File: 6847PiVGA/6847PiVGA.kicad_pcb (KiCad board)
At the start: 2 copper layers, 37 parts, among them J1 DB15_Female_HighDensity, U1 MC6847, U2 AD724JRZ, U4 AD813, Y1 4.433620MHz

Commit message: refine hardware layout
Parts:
- added U3: Pico, Package_DIP:DIP-42_W15.24mm, F.Cu at (90.9, 86.1)
- J1: footprint Resistor_SMD:R_0603_1608Metric -> Connector_Dsub:DSUB-15-HD_Female_Horizontal_P2.29x1.98mm_EdgePinOffset3.03mm_Housed_MountingHolesOffset4.94mm
- moved R6 79.6 mm to (111.8, 125.2), turned to 180 degrees
- moved C2 76.6 mm to (125.1, 133.7), turned to 180 degrees
- moved C8 75.0 mm to (126.4, 129.9), turned to 180 degrees
- moved R4 74.9 mm to (111.8, 119.1), turned to 180 degrees
- moved R12 74.7 mm to (115.8, 129.5)
- moved R2 72.1 mm to (111.8, 109.5), turned to 180 degrees
- moved U4 72.0 mm to (131.8, 107.2)
- moved R13 66.3 mm to (146.2, 135.0), turned to -90 degrees
- moved R5 66.1 mm to (111.8, 122.2), turned to 180 degrees
- moved R7 62.8 mm to (111.8, 129.5), turned to 180 degrees
- moved R9 59.9 mm to (111.8, 135.6), turned to 180 degrees
- moved C3 57.9 mm to (122.6, 132.0), turned to 180 degrees
- moved C4 57.5 mm to (122.0, 116.1)
- moved C9 55.4 mm to (146.2, 131.4), turned to -90 degrees
- moved C7 55.0 mm to (125.9, 119.3)
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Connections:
- C1 pad 2: Net-(C1-Pad2) -> Net-(J1-Pad3)
- C3 pad 2: Net-(C3-Pad2) -> Net-(J1-Pad1)
- J1 pad 1: Net-(C3-Pad2) -> Net-(J1-Pad1)
- R1 pad 1: Net-(C1-Pad2) -> Net-(J1-Pad1)
- R10 pad 1: Net-(C1-Pad2) -> Net-(J1-Pad1)
- R12 pad 1: Net-(C3-Pad2) -> Net-(J1-Pad3)
- R2 pad 1: Net-(C1-Pad2) -> Net-(J1-Pad1)
- R3 pad 1: Net-(C1-Pad2) -> Net-(J1-Pad1)
- R7 pad 1: Net-(C3-Pad2) -> Net-(J1-Pad3)
- R8 pad 1: Net-(C3-Pad2) -> Net-(J1-Pad3)
- R9 pad 1: Net-(C3-Pad2) -> Net-(J1-Pad3)
- U4 pad 10: Net-(C3-Pad2) -> Net-(J1-Pad3)
- U4 pad 5: Net-(C1-Pad2) -> Net-(J1-Pad1)
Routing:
- net +5V: track 0.00 -> 194.8 mm, vias 0 -> 2
- net Net-(J1-Pad14): track 0.00 -> 136.5 mm, vias 0 -> 2
- net Net-(J1-Pad13): track 0.00 -> 130.7 mm, vias 0 -> 3
- net GND: track 0.00 -> 84.7 mm, vias 0 -> 12
- net Net-(J1-Pad3): track 0.00 -> 84.1 mm, vias 0 -> 3
- net Net-(J1-Pad2): track 0.00 -> 80.2 mm, vias 0 -> 4
- net Net-(J1-Pad1): track 0.00 -> 72.5 mm, vias 0 -> 3
- net Net-(U1-Pad35): track 0.00 -> 41.1 mm
- net Net-(U1-Pad39): track 0.00 -> 37.8 mm
- net Net-(U1-Pad2): track 0.00 -> 33.5 mm
- net Net-(U1-Pad33): track 0.00 -> 28.0 mm
- net Net-(U1-Pad34): track 0.00 -> 27.0 mm
- net Net-(R19-Pad2): track 0.00 -> 13.1 mm
- net Net-(R18-Pad2): track 0.00 -> 12.9 mm
- net Net-(R17-Pad2): track 0.00 -> 11.1 mm
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- added copper zone on F.Cu, net GND
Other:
- board outline added: 69.6 x 59.2 mm

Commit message: board refresh
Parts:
- C1, C10, C2, C3, C4, C5, C6, C7, C8, C9: footprint Capacitor_SMD:C_0603_1608Metric -> Capacitor_SMD:C_0805_2012Metric
- R1, R10, R11, R12, R13, R14, R15, R16, R17, R18, R19, R20, R21, R22, R5, R8: footprint Resistor_SMD:R_0603_1608Metric -> Resistor_SMD:R_0805_2012Metric
- R2: value 1K -> 2K; footprint Resistor_SMD:R_0603_1608Metric -> Resistor_SMD:R_0805_2012Metric
- R3, R6, R9: value 2K -> 499R; footprint Resistor_SMD:R_0603_1608Metric -> Resistor_SMD:R_0805_2012Metric
- R4, R7: value 499R -> 2K; footprint Resistor_SMD:R_0603_1608Metric -> Resistor_SMD:R_0805_2012Metric
- moved R20 29.7 mm to (142.6, 91.9), turned to 180 degrees
- moved R17 25.3 mm to (142.6, 96.0)
- moved R14 24.9 mm to (142.6, 94.0), turned to 0 degrees
- moved R9 6.35 mm to (111.7, 129.3)
- moved R1 6.10 mm to (111.7, 112.5)
- moved R3 6.10 mm to (111.8, 106.4)
- moved R4 6.10 mm to (111.8, 125.2)
- moved R6 6.10 mm to (111.8, 119.1)
- moved R7 5.84 mm to (111.7, 135.4)
- moved R16 3.33 mm to (142.6, 111.8)
- moved R15 3.30 mm to (142.6, 102.7)
- moved R19 1.78 mm to (142.7, 114.3)
- moved R21 1.27 mm to (142.7, 100.6)
- moved C9 0.89 mm to (145.3, 131.4)
- moved R13 0.89 mm to (145.3, 135.0)
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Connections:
- net Net-(C1-Pad1) renamed /Bin
- net Net-(C2-Pad1) renamed /Gin
- net Net-(C3-Pad1) renamed /Rin
- net Net-(C9-Pad1) renamed /Composite
- net Net-(J1-Pad1) renamed Rvga
- net Net-(J1-Pad2) renamed Gvga
- net Net-(J1-Pad3) renamed Bvga
- net Net-(U1-Pad2) renamed DD6
- net Net-(U1-Pad22) renamed Atiming
- net Net-(U1-Pad27) renamed GM2
- net Net-(U1-Pad29) renamed GM1
- net Net-(U1-Pad3) renamed DD0
- net Net-(U1-Pad30) renamed GM0
- net Net-(U1-Pad33) renamed CLK
- net Net-(U1-Pad34) renamed DD7
- net Net-(U1-Pad35) renamed ~{A}/G
- net Net-(U1-Pad39) renamed CSS
- net Net-(U1-Pad4) renamed DD1
- net Net-(U1-Pad5) renamed DD2
- net Net-(U1-Pad6) renamed DD3
- net Net-(U1-Pad7) renamed DD4
- net Net-(U1-Pad8) renamed DD5
- J1 pad 10: unconnected-(J1-Pad10) -> GND
- J1 pad 13: Net-(J1-Pad13) -> Hsync
- J1 pad 14: Net-(J1-Pad14) -> Vsync
- J1 pad 5: unconnected-(J1-Pad5) -> GND
- J1 pad 7: unconnected-(J1-Pad7) -> GND
- U1 pad 12: Net-(J1-Pad13) -> Vsync
- U1 pad 37: Net-(J1-Pad13) -> Vsync
- U1 pad 38: Net-(J1-Pad14) -> Hsync
- U2 pad 15: Net-(J1-Pad13) -> Vsync
- U2 pad 16: Net-(J1-Pad14) -> Hsync
- U3 pad 17: Net-(J1-Pad13) -> Vsync
- U3 pad 18: unconnected-(U3-Pad18) -> GND
- U3 pad 21: Net-(J1-Pad14) -> Hsync
- U3 pad 22: Net-(R9-Pad2) -> Net-(R7-Pad2)
- U3 pad 23: unconnected-(U3-Pad23) -> GND
- U3 pad 25: Net-(R7-Pad2) -> Net-(R9-Pad2)
- U3 pad 26: Net-(R6-Pad2) -> Net-(R4-Pad2)
- U3 pad 28: unconnected-(U3-Pad28) -> GND
- U3 pad 29: Net-(R4-Pad2) -> Net-(R6-Pad2)
- U3 pad 3: unconnected-(U3-Pad3) -> GND
- U3 pad 31: Net-(R3-Pad2) -> Net-(R1-Pad2)
- U3 pad 33: unconnected-(U3-Pad33) -> GND
- U3 pad 34: Net-(R1-Pad2) -> Net-(R3-Pad2)
- U3 pad 39: unconnected-(U3-Pad39) -> +5V
- U3 pad 40: +5V -> unconnected-(U3-Pad40)
- U3 pad 8: unconnected-(U3-Pad8) -> GND
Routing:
- net GND: track 84.7 -> 223.6 mm
- net Net-(J1-Pad14): track 136.5 -> 0.00 mm, vias 2 -> 0
- net Hsync: track 0.00 -> 134.2 mm, vias 0 -> 2
- net Vsync: track 0.00 -> 133.1 mm, vias 0 -> 3
- net Net-(J1-Pad13): track 130.7 -> 0.00 mm, vias 3 -> 0
- net Net-(R14-Pad1): track 7.93 -> 27.1 mm, vias 0 -> 2
- net Net-(R17-Pad2): track 11.1 -> 29.4 mm, vias 0 -> 2
- net Net-(R19-Pad2): track 13.1 -> 15.9 mm
- net Net-(R16-Pad1): track 8.25 -> 10.0 mm
- net Net-(R15-Pad1): track 8.25 -> 9.92 mm
- net Bvga: track 84.1 -> 85.3 mm
- net /Composite: track 4.24 -> 3.19 mm
- net Rvga: track 72.5 -> 71.5 mm
- net Net-(R18-Pad2): track 12.9 -> 13.9 mm
- net Gvga: track 80.2 -> 81.2 mm
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
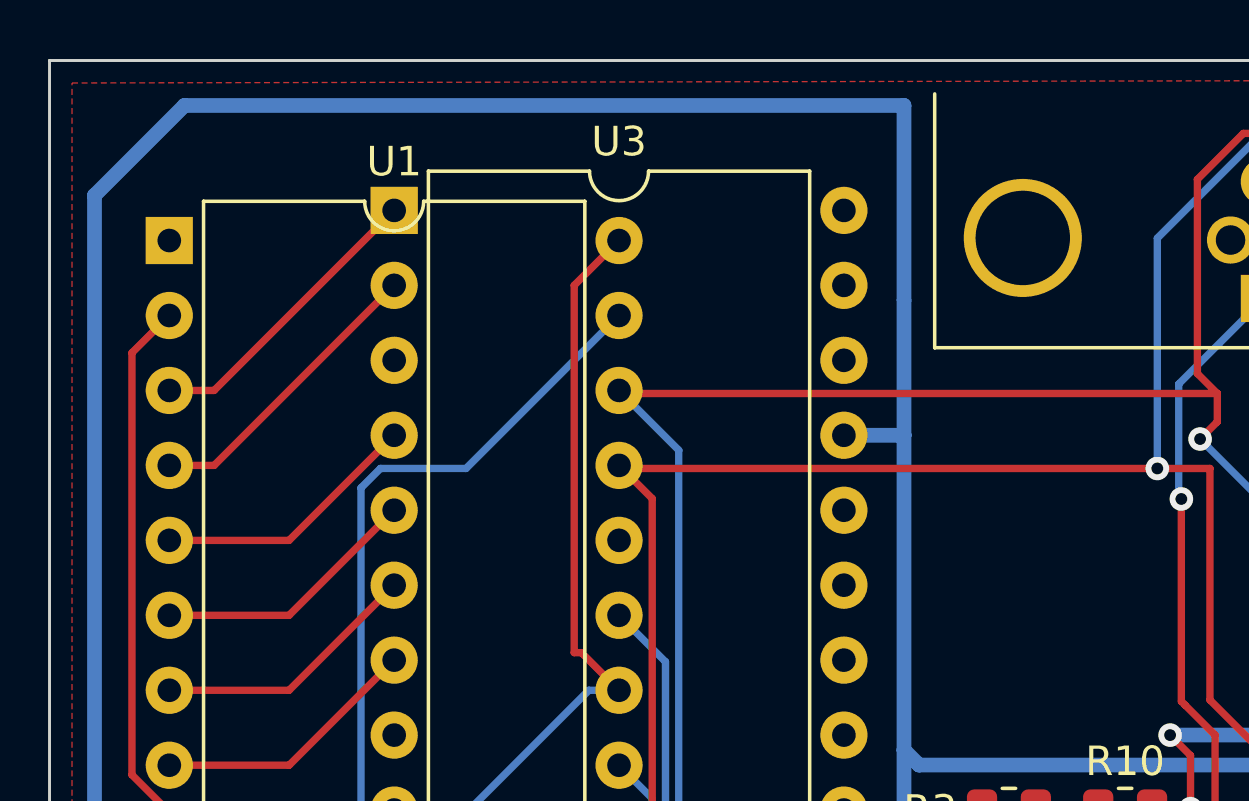
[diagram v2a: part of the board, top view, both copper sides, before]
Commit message: add power protection
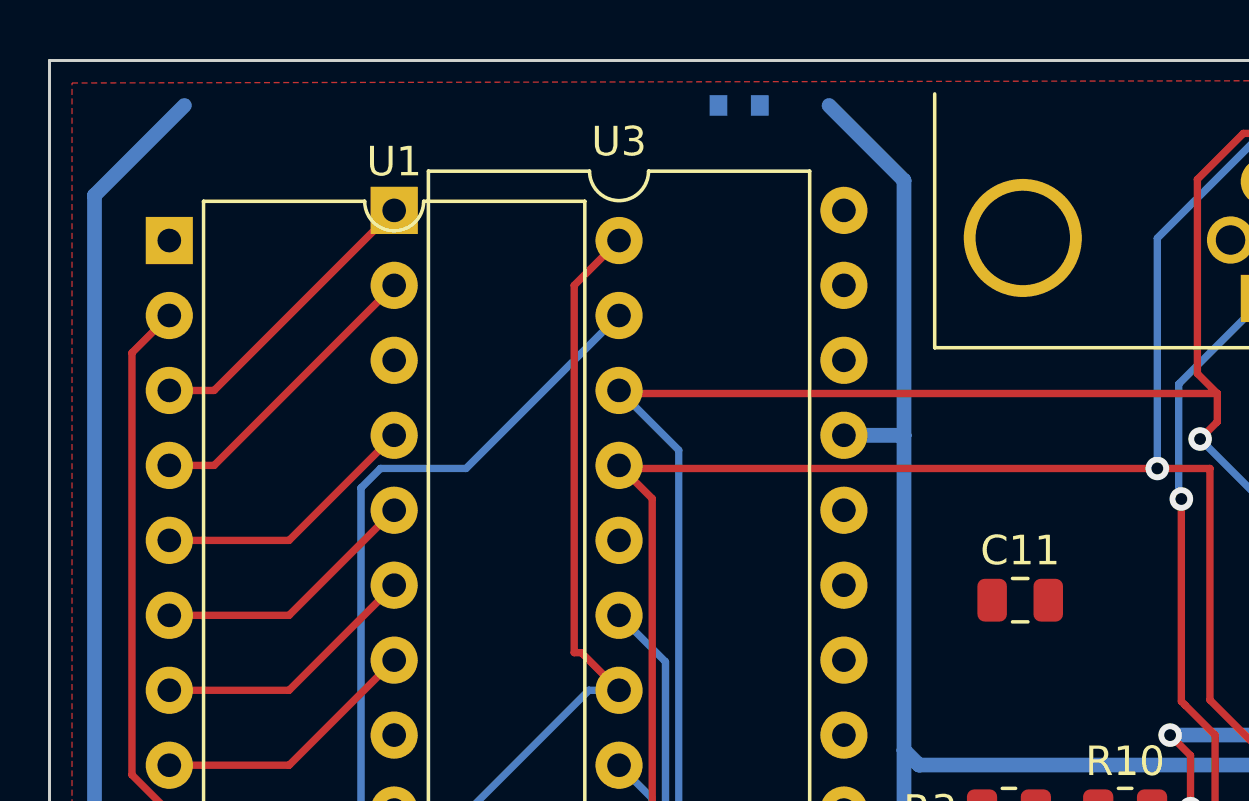
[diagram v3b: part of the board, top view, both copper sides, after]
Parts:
- added C11: 10uF, Capacitor_SMD:C_0805_2012Metric, F.Cu at (112.1, 99.3)
- added D1: 1N5817, Diode_SMD:D_SOD-523, B.Cu at (102.6, 82.5)
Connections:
- U3 pad 39: +5V -> Net-(U3-Pad39)
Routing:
- net +5V: track 194.9 -> 171.5 mm
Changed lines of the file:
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@@
   (net 78 "unconnected-(U3-Pad40)")
   (net 79 "/Composite")
+  (net 80 "Net-(U3-Pad39)")
   (footprint "Resistor_SMD:R_0805_2012Metric" (layer "F.Cu")
     (at 111.76 119.126 180)
@@
     )
   )
+  (footprint "Capacitor_SMD:C_0805_2012Metric" (layer "F.Cu")
+    (at 112.141 99.314)
+    (descr "Capacitor SMD 0805 (2012 Metric), square (rectangular) end terminal, IPC_7351 nominal, (Body size source: IPC-SM-782 page 76, https://www.pcb-3d.com/wordpress/wp-content/uploads/ipc-sm-782a_amendment_1_and_2.pdf, https://docs.google.com/spreadsheets/d/1BsfQQcO9C6DZCsRaXUlFlo91Tg2WpOkGARC1WS5S8t0/edit?usp=sharing), generated with kicad-footprint-generator")
+    (tags "capacitor")
+    (property "Sheetfile" "6847PiVGA.kicad_sch")
+    (property "Sheetname" "")
+    (attr smd)
+    (fp_text reference "C11" (at 0 -1.68) (layer "F.SilkS")
+      (effects (font (size 1 1) (thickness 0.15)))
+    )
+    (fp_text value "10uF" (at 0 1.68) (layer "F.Fab")
+      (effects (font (size 1 1) (thickness 0.15)))
+    )
+    (fp_text user "${REFERENCE}" (at 0 0) (layer "F.Fab")
+      (effects (font (size 0.5 0.5) (thickness 0.08)))
+    )
+    (fp_line (start -0.261252 0.735) (end 0.261252 0.735) (layer "F.SilkS") (width 0.12))
+    (fp_line (start -0.261252 -0.735) (end 0.261252 -0.735) (layer "F.SilkS") (width 0.12))
+    (fp_line (start 1.7 -0.98) (end 1.7 0.98) (layer "F.CrtYd") (width 0.05))
+    (fp_line (start -1.7 -0.98) (end 1.7 -0.98) (layer "F.CrtYd") (width 0.05))
+    (fp_line (start -1.7 0.98) (end -1.7 -0.98) (layer "F.CrtYd") (width 0.05))
+    (fp_line (start 1.7 0.98) (end -1.7 0.98) (layer "F.CrtYd") (width 0.05))
+    (fp_line (start 1 0.625) (end -1 0.625) (layer "F.Fab") (width 0.1))
+    (fp_line (start -1 0.625) (end -1 -0.625) (layer "F.Fab") (width 0.1))
+    (fp_line (start -1 -0.625) (end 1 -0.625) (layer "F.Fab") (width 0.1))
+    (fp_line (start 1 -0.625) (end 1 0.625) (layer "F.Fab") (width 0.1))
+    (pad "1" smd roundrect (at -0.95 0) (size 1 1.45) (layers "F.Cu" "F.Paste" "F.Mask") (roundrect_rratio 0.25)
+      (net 1 "+5V") (pintype "passive"))
+    (pad "2" smd roundrect (at 0.95 0) (size 1 1.45) (layers "F.Cu" "F.Paste" "F.Mask") (roundrect_rratio 0.25)
+      (net 2 "GND") (pintype "passive"))
+    (model "${KICAD6_3DMODEL_DIR}/Capacitor_SMD.3dshapes/C_0805_2012Metric.wrl"
+      (offset (xyz 0 0 0))
+      (scale (xyz 1 1 1))
+      (rotate (xyz 0 0 0))
+    )
+  )
   (footprint "Resistor_SMD:R_0805_2012Metric" (layer "F.Cu")
     (at 142.683 109.474 180)
@@
       (net 2 "GND") (pinfunction "GND") (pintype "bidirectional"))
     (pad "39" thru_hole oval (at 15.24 7.62) (size 1.6 1.6) (drill 0.8) (layers *.Cu *.Mask)
-      (net 1 "+5V") (pinfunction "VSYS") (pintype "unspecified"))
+      (net 80 "Net-(U3-Pad39)") (pinfunction "VSYS") (pintype "unspecified"))
     (pad "40" thru_hole oval (at 15.24 5.08) (size 1.6 1.6) (drill 0.8) (layers *.Cu *.Mask)
       (net 78 "unconnected-(U3-Pad40)") (pinfunction "VBUS") (pintype "unspecified+no_connect"))
@@
     )
   )
+  (footprint "Diode_SMD:D_SOD-523" (layer "B.Cu")
+    (at 102.616 82.55 180)
+    (descr "http://www.diodes.com/datasheets/ap02001.pdf p.144")
+    (tags "Diode SOD523")
+    (property "Sheetfile" "6847PiVGA.kicad_sch")
+    (property "Sheetname" "")
+    (attr smd)
+    (fp_text reference "D1" (at 0 1.3) (layer "B.SilkS")
+      (effects (font (size 1 1) (thickness 0.15)) (justify mirror))
+    )
+    (fp_text value "1N5817" (at 0 -1.4) (layer "B.Fab")
+      (effects (font (size 1 1) (thickness 0.15)) (justify mirror))
+    )
+    (fp_text user "${REFERENCE}" (at 0 1.3) (layer "B.Fab")
+      (effects (font (size 1 1) (thickness 0.15)) (justify mirror))
+    )
+    (fp_line (start -1.15 0.6) (end -1.15 -0.6) (layer "B.SilkS") (width 0.12))
+    (fp_line (start 0.7 -0.6) (end -1.15 -0.6) (layer "B.SilkS") (width 0.12))
+    (fp_line (start 0.7 0.6) (end -1.15 0.6) (layer "B.SilkS") (width 0.12))
+    (fp_line (start 1.25 -0.7) (end -1.25 -0.7) (layer "B.CrtYd") (width 0.05))
+    (fp_line (start -1.25 -0.7) (end -1.25 0.7) (layer "B.CrtYd") (width 0.05))
+    (fp_line (start 1.25 0.7) (end 1.25 -0.7) (layer "B.CrtYd") (width 0.05))
+    (fp_line (start -1.25 0.7) (end 1.25 0.7) (layer "B.CrtYd") (width 0.05))
+    (fp_line (start 0.1 0) (end 0.25 0) (layer "B.Fab") (width 0.1))
+    (fp_line (start 0.65 -0.45) (end -0.65 -0.45) (layer "B.Fab") (width 0.1))
+    (fp_line (start 0.65 0.45) (end 0.65 -0.45) (layer "B.Fab") (width 0.1))
+    (fp_line (start 0.1 0.2) (end -0.2 0) (layer "B.Fab") (width 0.1))
+    (fp_line (start -0.2 -0.2) (end -0.2 0.2) (layer "B.Fab") (width 0.1))
+    (fp_line (start -0.2 0) (end -0.35 0) (layer "B.Fab") (width 0.1))
+    (fp_line (start -0.65 0.45) (end 0.65 0.45) (layer "B.Fab") (width 0.1))
+    (fp_line (start 0.1 -0.2) (end 0.1 0.2) (layer "B.Fab") (width 0.1))
+    (fp_line (start -0.2 0) (end 0.1 -0.2) (layer "B.Fab") (width 0.1))
+    (fp_line (start -0.65 -0.45) (end -0.65 0.45) (layer "B.Fab") (width 0.1))
+    (pad "1" smd rect (at -0.7 0) (size 0.6 0.7) (layers "B.Cu" "B.Paste" "B.Mask")
+      (net 80 "Net-(U3-Pad39)") (pinfunction "K") (pintype "passive"))
+    (pad "2" smd rect (at 0.7 0) (size 0.6 0.7) (layers "B.Cu" "B.Paste" "B.Mask")
+      (net 1 "+5V") (pinfunction "A") (pintype "passive"))
+    (model "${KICAD6_3DMODEL_DIR}/Diode_SMD.3dshapes/D_SOD-523.wrl"
+      (offset (xyz 0 0 0))
+      (scale (xyz 1 1 1))
+      (rotate (xyz 0 0 0))
+    )
+  )
   (gr_rect (start 79.248 81.026) (end 148.844 140.208) (layer "Edge.Cuts") (width 0.1) (fill none))
   (segment (start 133.858 126.746) (end 132.588 126.746) (width 0.5) (layer "F.Cu") (net 1))
@@
   (via (at 121.92 104.902) (size 0.8) (drill 0.4) (layers "F.Cu" "B.Cu") (net 1))
   (via (at 121.158 117.602) (size 0.8) (drill 0.4) (layers "F.Cu" "B.Cu") (net 1))
-  (segment (start 80.772 85.598) (end 83.82 82.55) (width 0.5) (layer "B.Cu") (net 1))
   (segment (start 106.167 93.726) (end 108.204 93.726) (width 0.5) (layer "B.Cu") (net 1))
   (segment (start 108.712 117.602) (end 121.158 117.602) (width 0.5) (layer "B.Cu") (net 1))
-  (segment (start 108.204 89.149) (end 108.204 93.726) (width 0.5) (layer "B.Cu") (net 1))
-  (segment (start 83.82 82.55) (end 108.204 82.55) (width 0.5) (layer "B.Cu") (net 1))
   (segment (start 108.712 104.902) (end 121.92 104.902) (width 0.5) (layer "B.Cu") (net 1))
   (segment (start 108.204 93.726) (end 108.204 104.394) (width 0.5) (layer "B.Cu") (net 1))
+  (segment (start 105.664 82.55) (end 108.204 85.09) (width 0.5) (layer "B.Cu") (net 1))
+  (segment (start 80.772 85.598) (end 83.82 82.55) (width 0.5) (layer "B.Cu") (net 1))
   (segment (start 108.204 104.394) (end 108.204 117.094) (width 0.5) (layer "B.Cu") (net 1))
+  (segment (start 83.307 127.767) (end 80.772 125.232) (width 0.5) (layer "B.Cu") (net 1))
   (segment (start 108.204 104.394) (end 108.712 104.902) (width 0.5) (layer "B.Cu") (net 1))
+  (segment (start 108.204 117.094) (end 108.712 117.602) (width 0.5) (layer "B.Cu") (net 1))
   (segment (start 80.772 125.232) (end 80.772 85.598) (width 0.5) (layer "B.Cu") (net 1))
-  (segment (start 108.204 82.55) (end 108.204 89.149) (width 0.5) (layer "B.Cu") (net 1))
-  (segment (start 108.204 117.094) (end 108.712 117.602) (width 0.5) (layer "B.Cu") (net 1))
-  (segment (start 83.307 127.767) (end 80.772 125.232) (width 0.5) (layer "B.Cu") (net 1))
+  (segment (start 108.204 85.09) (end 108.204 93.726) (width 0.5) (layer "B.Cu") (net 1))
   (segment (start 124.907 119.253) (end 122.997 119.253) (width 0.25) (layer "F.Cu") (net 2))
   (segment (start 125.308 122.936) (end 132.588 122.936) (width 0.5) (layer "F.Cu") (net 2))
@@
   (via (at 144.399 124.206) (size 0.8) (drill 0.4) (layers "F.Cu" "B.Cu") (net 25))
   (segment (start 140.081 124.206) (end 144.399 124.206) (width 0.25) (layer "B.Cu") (net 25))
-  (segment (start 120.015 83.82) (end 125.974669 83.82) (width 0.25) (layer "B.Cu") (net 25))
   (segment (start 116.787989 94.850511) (end 116.787989 87.047011) (width 0.25) (layer "B.Cu") (net 25))
   (segment (start 116.787989 87.047011) (end 120.015 83.82) (width 0.25) (layer "B.Cu") (net 25))
+  (segment (start 120.015 83.82) (end 125.974669 83.82) (width 0.25) (layer "B.Cu") (net 25))
+  (segment (start 123.571 107.696) (end 140.081 124.206) (width 0.25) (layer "B.Cu") (net 25))
   (segment (start 125.974669 83.82) (end 127.284 85.129331) (width 0.25) (layer "B.Cu") (net 25))
-  (segment (start 123.571 107.696) (end 140.081 124.206) (width 0.25) (layer "B.Cu") (net 25))
   (segment (start 90.823489 106.322489) (end 90.927 106.426) (width 0.25) (layer "F.Cu") (net 26))
   (segment (start 83.132189 106.322489) (end 90.823489 106.322489) (width 0.25) (layer "F.Cu") (net 26))

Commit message: correct pico footprint
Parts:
- added J2: Conn_01x06_Male, Connector_PinHeader_2.54mm:PinHeader_1x06_P2.54mm_Vertical, F.Cu at (146.8, 109.7)
- C11: moved to B.Cu
- U3: footprint Package_DIP:DIP-42_W15.24mm -> Package_DIP:DIP-40_W15.24mm
- moved C11 12.4 mm to (102.8, 91.2)
- moved R11 3.61 mm to (115.1, 115.6)
- moved R5 3.61 mm to (111.1, 118.6)
- moved R6 3.61 mm to (111.1, 115.6)
- moved R4 3.61 mm to (111.1, 121.7)
- moved R1 3.60 mm to (111.1, 109.0)
- moved R2 3.60 mm to (111.2, 105.9)
- moved R3 3.60 mm to (111.2, 102.9)
- moved R10 3.60 mm to (115.1, 102.9)
- moved R7 3.60 mm to (111.1, 131.8)
- moved R8 3.60 mm to (111.1, 128.8)
- moved R12 3.60 mm to (115.3, 126.1)
- moved R9 3.60 mm to (111.1, 125.7)
- moved D1 0.89 mm to (102.6, 83.4)
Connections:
- C10 pad 1: +5V -> +5VD
- C4 pad 1: +5V -> +5VD
- C5 pad 2: +5V -> +5VD
- C6 pad 1: +5V -> +5VD
- C7 pad 2: +5V -> +5VD
- D1 pad 1: Net-(U3-Pad39) -> +5VD
- U2 pad 14: +5V -> +5VD
- U2 pad 4: +5V -> +5VD
- U2 pad 5: +5V -> +5VD
- U3 pad 39: Net-(U3-Pad39) -> +5VD
- U4 pad 4: +5V -> +5VD
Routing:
- net +5VD: track 0.00 -> 122.0 mm, vias 0 -> 2
- net +5V: track 171.5 -> 73.0 mm, vias 2 -> 0
- net GND: track 223.6 -> 177.4 mm, vias 12 -> 10
- net B: track 0.00 -> 17.1 mm
- net Comp: track 0.00 -> 14.1 mm
- net G: track 0.00 -> 10.9 mm
- net Hsync: track 134.2 -> 125.5 mm
- net R: track 0.00 -> 4.54 mm
- net Gvga: track 81.2 -> 79.4 mm
- net Rvga: track 71.5 -> 73.0 mm
- net Net-(R4-Pad2): track 5.40 -> 4.07 mm
- net Net-(R5-Pad2): track 5.61 -> 4.28 mm
- net Net-(R2-Pad2): track 5.61 -> 4.32 mm
- net Net-(R1-Pad2): track 5.34 -> 4.05 mm
- net Net-(R7-Pad2): track 5.34 -> 4.07 mm
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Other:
- board text added: "6847PI VGA"
- board text added: "6847PI VGA Revision 2"
- board text added: "By Julian Brown"

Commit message: autorouted
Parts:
- moved J2 12.9 mm to (143.5, 122.2)
- moved C9 5.85 mm to (139.4, 131.1)
- moved R13 5.85 mm to (139.4, 134.7)
- moved U2 5.85 mm to (134.6, 122.2)
- moved C3 2.59 mm to (120.0, 131.4)
- moved Y1 2.59 mm to (122.4, 125.0)
- moved C1 2.59 mm to (125.1, 135.0)
- moved C2 2.59 mm to (122.6, 133.2)
- moved C8 2.59 mm to (123.8, 129.4)
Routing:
- net B: track 17.1 -> 49.7 mm
- net GND: track 177.4 -> 147.7 mm, vias 10 -> 8
- net G: track 10.9 -> 32.4 mm
- net +5VD: track 122.0 -> 106.0 mm
- net R: track 4.54 -> 16.7 mm
- net Bvga: track 86.3 -> 75.0 mm, vias 4 -> 2
- net Comp: track 14.1 -> 4.36 mm
- net CLK: track 28.0 -> 22.6 mm
- net Vsync: track 133.1 -> 127.8 mm, vias 3 -> 1
- net DD6: track 33.5 -> 28.3 mm
- net Gvga: track 79.4 -> 74.2 mm, vias 4 -> 1
- net /Bin: track 5.70 -> 10.7 mm
- net ~{A}/G: track 41.1 -> 36.8 mm
- net Hsync: track 125.5 -> 121.2 mm, vias 2 -> 0
- net Rvga: track 73.0 -> 68.9 mm, vias 3 -> 0
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- added copper zone on B.Cu, net GND
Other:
- board size 69.6 x 59.2 mm -> 68.1 x 57.7 mm
